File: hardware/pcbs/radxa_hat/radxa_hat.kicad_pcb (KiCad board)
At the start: 2 copper layers, 1 part, among them J1 RADXA_HEADER

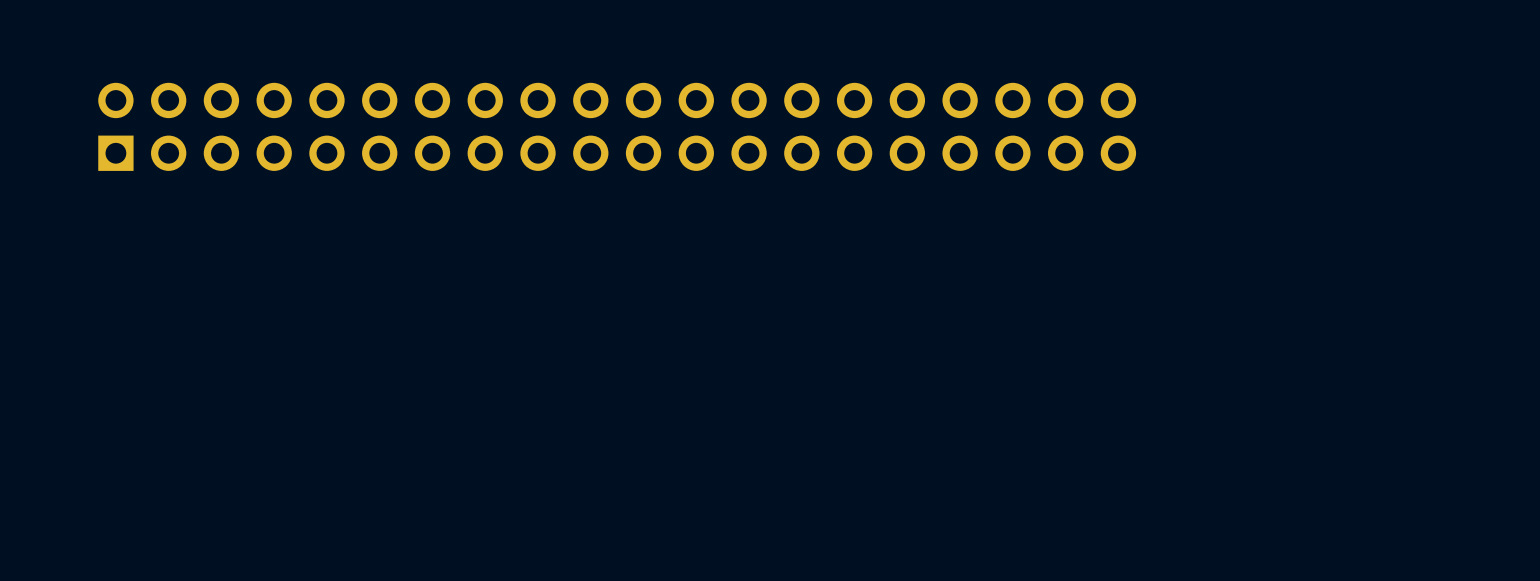
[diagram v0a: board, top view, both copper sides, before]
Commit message: hats_pcbs: add some connectors
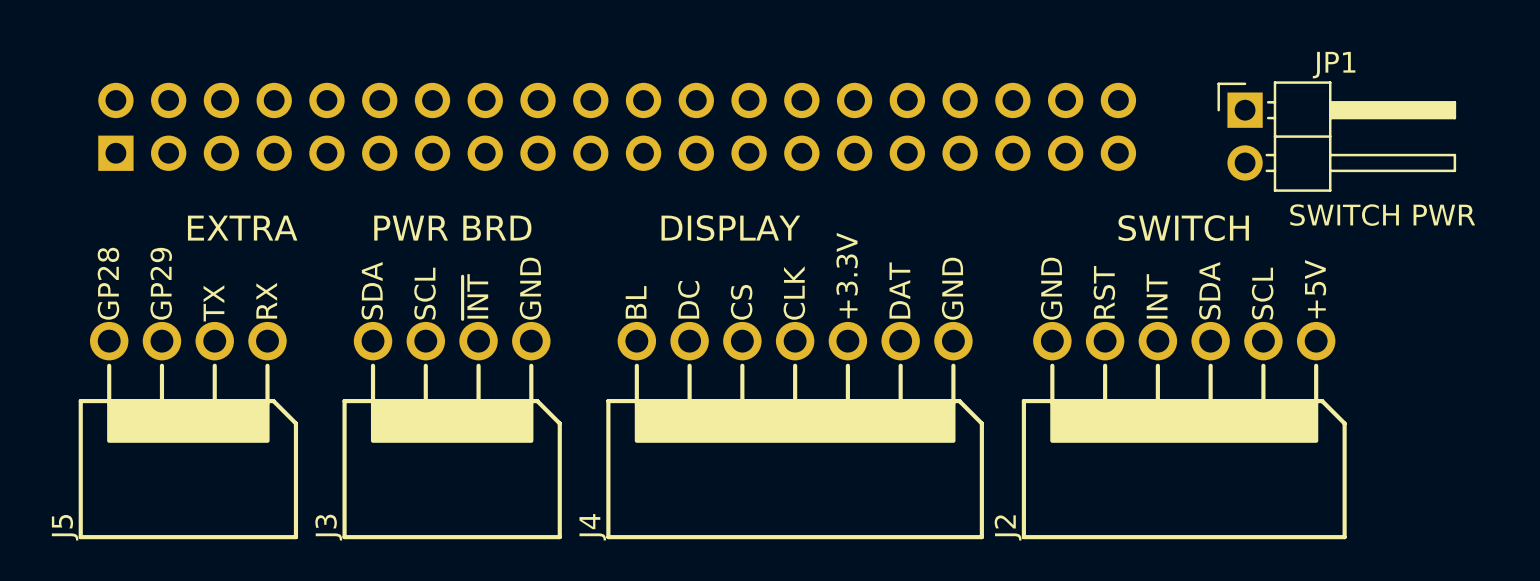
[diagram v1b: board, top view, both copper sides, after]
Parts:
- added J2: Header_01x06, Connector_MTA-100:mta100_01x6_P2.54_640455-6, F.Cu at (132.1, 57.8)
- added J3: Header_01x04, Connector_MTA-100:mta100_01x4_P2.54_640455-4, F.Cu at (99.4, 57.8)
- added J4: Header_01x06, Connector_MTA-100:mta100_01x7_P2.54_640455-7, F.Cu at (112.1, 57.8)
- added J5: Header_01x04, Connector_MTA-100:mta100_01x4_P2.54_640455-4, F.Cu at (86.7, 57.8)
- added JP1: SWITCH PWR, Connector_PinHeader_2.54mm:PinHeader_1x02_P2.54mm_Horizontal, F.Cu at (141.4, 46.7)
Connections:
- J1 pad 1: unconnected-(J1-+3.3V-Pad1) -> +3.3V
- J1 pad 11: unconnected-(J1-GP05-Pad11) -> /EXTRA_RX
- J1 pad 14: unconnected-(J1-GND-Pad14) -> GND
- J1 pad 16: unconnected-(J1-GP22-Pad16) -> /DISP_BL
- J1 pad 17: unconnected-(J1-+3.3V-Pad17) -> +3.3V
- J1 pad 18: unconnected-(J1-GP27-Pad18) -> /PWR_BRD_SCL
- J1 pad 19: unconnected-(J1-GP11-Pad19) -> /DISP_DAT
- J1 pad 2: unconnected-(J1-+5V-Pad2) -> +5V
- J1 pad 20: unconnected-(J1-GND-Pad20) -> GND
- J1 pad 23: unconnected-(J1-GP10-Pad23) -> /DISP_CLK
- J1 pad 25: unconnected-(J1-GND-Pad25) -> GND
- J1 pad 26: unconnected-(J1-GP18-Pad26) -> /PWR_BRD_INT
- J1 pad 28: unconnected-(J1-GP17-Pad28) -> /PWR_BRD_INT
- J1 pad 3: unconnected-(J1-GP28-Pad3) -> /EXTRA_GP28
- J1 pad 30: unconnected-(J1-GND-Pad30) -> GND
- J1 pad 32: unconnected-(J1-GP19-Pad32) -> /DISP_DC
- J1 pad 33: unconnected-(J1-GP13-Pad33) -> /DISP_CS
- J1 pad 34: unconnected-(J1-GND-Pad34) -> GND
- J1 pad 35: unconnected-(J1-GP15-Pad35) -> /NSW_SCL
- J1 pad 36: unconnected-(J1-GP26-Pad36) -> /PWR_BRD_SDA
- J1 pad 37: unconnected-(J1-GP14-Pad37) -> /NSW_SDA
- J1 pad 38: unconnected-(J1-GP02-Pad38) -> /NSW_INT
- J1 pad 39: unconnected-(J1-GND-Pad39) -> GND
- J1 pad 4: unconnected-(J1-+5V-Pad4) -> +5V
- J1 pad 40: unconnected-(J1-GP25-Pad40) -> /NSW_RST
- J1 pad 5: unconnected-(J1-GP29-Pad5) -> /EXTRA_GP29
- J1 pad 6: unconnected-(J1-GND-Pad6) -> GND
- J1 pad 7: unconnected-(J1-GP04-Pad7) -> /EXTRA_TX
- J1 pad 8: unconnected-(J1-GP20-Pad8) -> /DISP_RST
- J1 pad 9: unconnected-(J1-GND-Pad9) -> GND

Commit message: hat_pcbs are almost done
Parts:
- added H1: MountingHole_Pad, MountingHole:MountingHole_3.2mm_M3_DIN965_Pad, F.Cu at (135.0, 88.9)
- added H2: MountingHole_Pad, MountingHole:MountingHole_3.2mm_M3_DIN965_Pad, F.Cu at (77.0, 88.9)
- J4: value Header_01x06 -> Header_01x08; footprint Connector_MTA-100:mta100_01x7_P2.54_640455-7 -> Connector_MTA-100:mta100_01x8_P2.54_640455-8
- JP1: footprint Connector_PinHeader_2.54mm:PinHeader_1x02_P2.54mm_Horizontal -> Connector_PinHeader_2.54mm:PinHeader_1x02_P2.54mm_Vertical
- moved JP1 53.0 mm to (119.4, 94.9)
- moved J3 45.2 mm to (88.3, 101.6)
- moved J4 45.2 mm to (101.0, 101.6)
- moved J5 45.2 mm to (75.6, 101.6)
- moved J2 44.6 mm to (123.8, 101.6)
- moved J1 41.7 mm to (81.9, 90.2)
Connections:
- J2 pad 1: Net-(J2-Pin_1) -> GND
- J2 pad 2: /NSW_SDA -> /NSW_RST
- J2 pad 3: /NSW_SCL -> /NSW_INT
- J2 pad 4: /NSW_INT -> /NSW_SCL
- J2 pad 5: /NSW_RST -> /NSW_SDA
- J2 pad 6: GND -> Net-(J2-Pin_6)
- J3 pad 1: GND -> /PWR_BRD_SDA
- J3 pad 2: /PWR_BRD_INT -> /PWR_BRD_SCL
- J3 pad 3: /PWR_BRD_SCL -> /PWR_BRD_INT
- J3 pad 4: /PWR_BRD_SDA -> GND
- J4 pad 3: /DISP_DAT -> /DISP_CS
- J4 pad 4: /DISP_CLK -> /DISP_DC
- J4 pad 5: /DISP_CS -> /DISP_CLK
- J4 pad 6: /DISP_DC -> /DISP_DAT
- JP1 pad 1: Net-(J2-Pin_1) -> Net-(J2-Pin_6)
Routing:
- net +3.3V: track 0.00 -> 68.8 mm
- net +5V: track 0.00 -> 63.5 mm
- net /PWR_BRD_SDA: track 0.00 -> 40.7 mm
- net /PWR_BRD_INT: track 0.00 -> 35.4 mm, vias 0 -> 1
- net /DISP_DC: track 0.00 -> 20.3 mm
- net /DISP_RST: track 0.00 -> 20.2 mm
- net /EXTRA_RX: track 0.00 -> 19.0 mm
- net /DISP_CS: track 0.00 -> 18.8 mm
- net /EXTRA_GP29: track 0.00 -> 18.6 mm
- net /EXTRA_GP28: track 0.00 -> 18.6 mm
- net /EXTRA_TX: track 0.00 -> 17.7 mm
- net /PWR_BRD_SCL: track 0.00 -> 17.7 mm
- net /NSW_SCL: track 0.00 -> 16.6 mm
- net /DISP_BL: track 0.00 -> 15.5 mm
- net /NSW_RST: track 0.00 -> 15.5 mm
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- added copper zone on B.Cu, net GND
- added copper zone on F.Cu, net GND
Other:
- board outline added: 65 x 26.5 mm

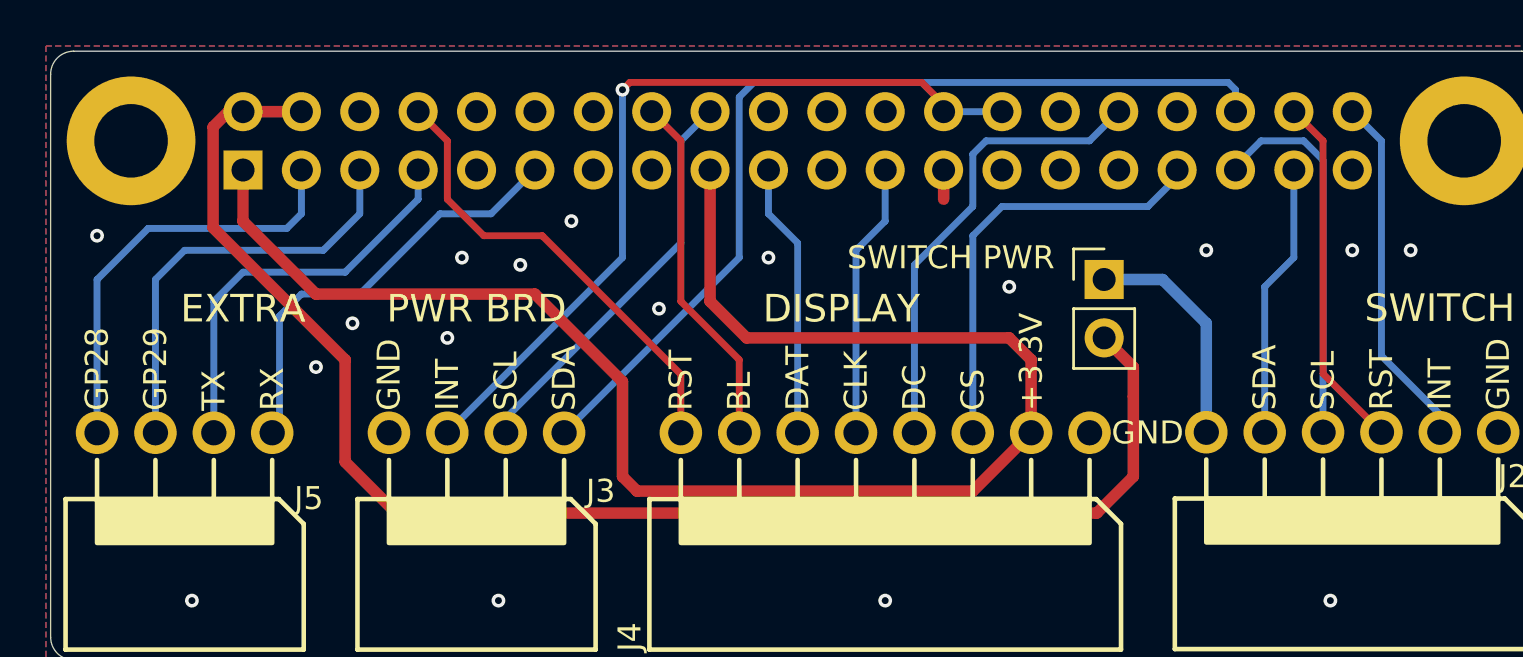
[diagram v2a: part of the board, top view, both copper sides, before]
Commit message: hat_pcbs: add some resistors
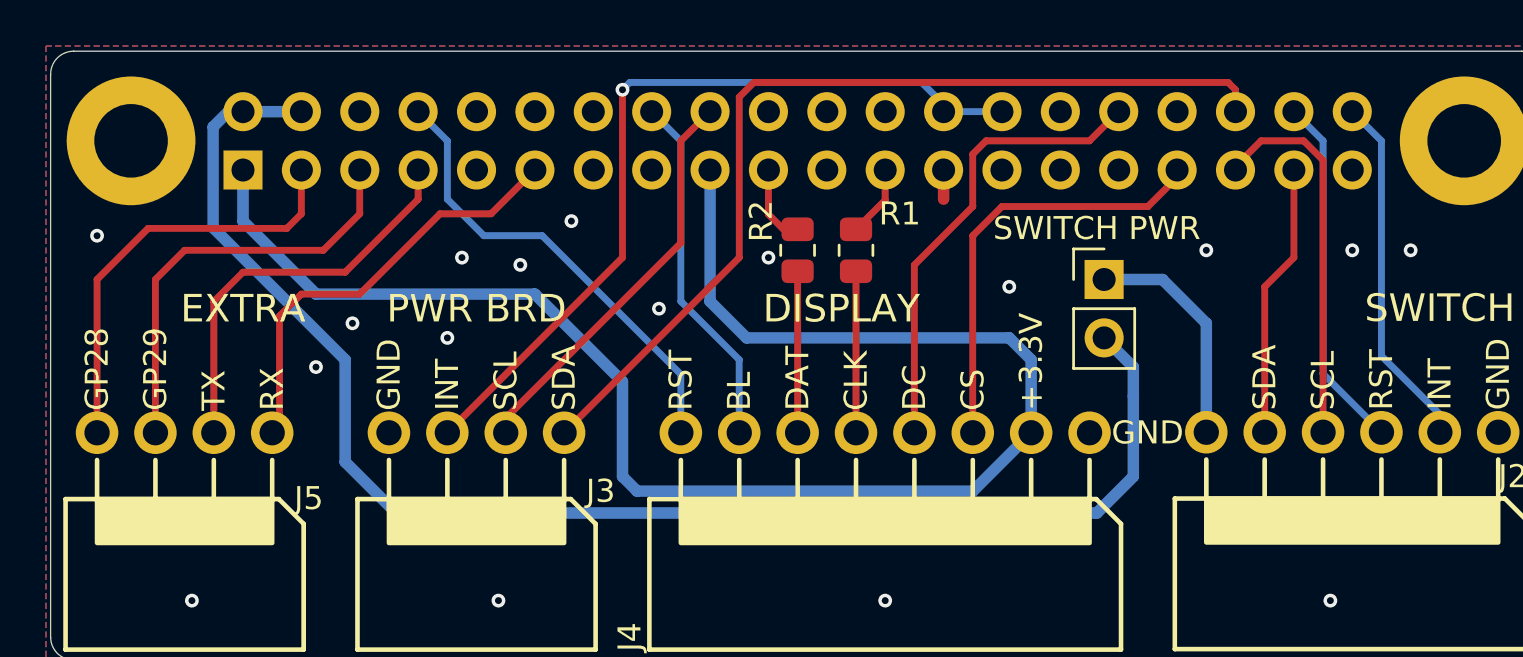
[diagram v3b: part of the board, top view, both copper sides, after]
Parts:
- added R1: 1Ω, Resistor_SMD:R_0805_2012Metric, F.Cu at (108.6, 93.7)
- added R2: 1Ω, Resistor_SMD:R_0805_2012Metric, F.Cu at (106.0, 93.7)
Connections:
- J4 pad 5: /DISP_CLK -> Net-(J4-Pin_5)
- J4 pad 6: /DISP_DAT -> Net-(J4-Pin_6)
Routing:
- net /DISP_CLK: track 12.0 -> 3.11 mm
- net /DISP_DAT: track 12.0 -> 3.47 mm
- net Net-(J4-Pin_6): track 0.00 -> 7.02 mm
- net Net-(J4-Pin_5): track 0.00 -> 7.02 mm

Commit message: hat_pcbs: final changes
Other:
- board text added: "FOSDEM radxa hat rev. A"
- board text added: "JLCJLCJLCJLC"
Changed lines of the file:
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@@
 	)
 	(paper "A4")
+	(title_block
+		(comment 4 "AISLER Project ID: AAMJXCDQ")
+	)
 	(layers
 		(0 "F.Cu" signal)
@@
 		(layer "Edge.Cuts")
 	)
+	(gr_text "JLCJLCJLCJLC"
+		(at 95.25 105.7275 180)
+		(layer "B.SilkS")
+		(effects
+			(font
+				(size 1 1)
+				(thickness 0.1)
+			)
+			(justify left bottom mirror)
+		)
+	)
+	(gr_text "FOSDEM radxa hat rev. A"
+		(at 90.4875 107.315 180)
+		(layer "B.SilkS")
+		(effects
+			(font
+				(size 1 1)
+				(thickness 0.1)
+			)
+			(justify left bottom mirror)
+		)
+	)
 	(segment

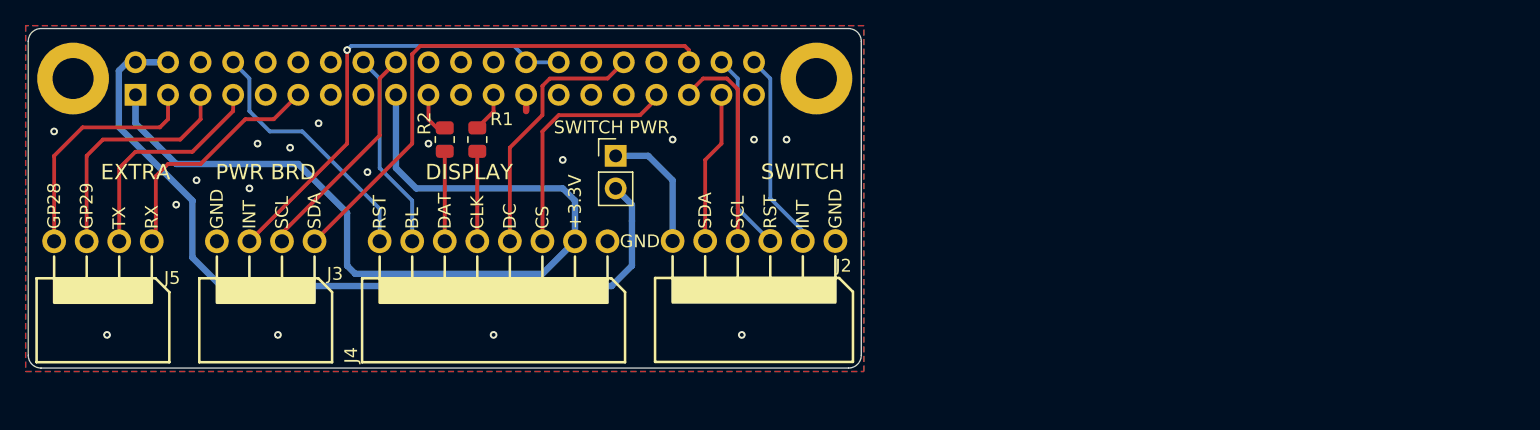
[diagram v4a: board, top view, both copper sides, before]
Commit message: boards: update fabrication output settings
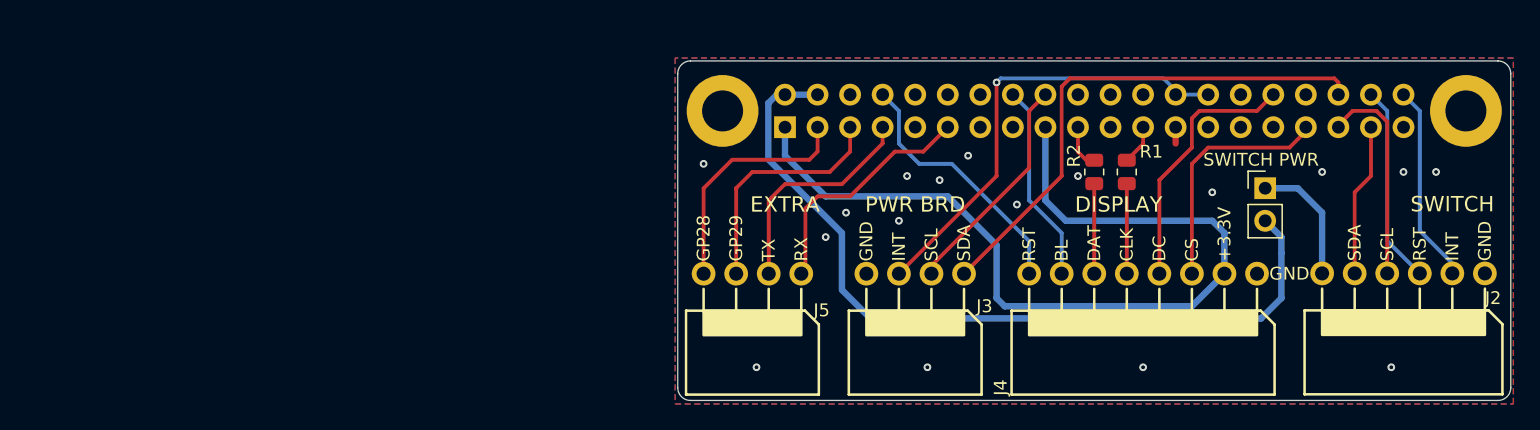
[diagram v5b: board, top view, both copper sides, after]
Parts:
- moved H1 50.7 mm to (185.7, 91.4)
- moved J4 50.7 mm to (151.6, 104.1)
- moved J5 50.7 mm to (126.2, 104.1)
- moved JP1 50.7 mm to (170.1, 97.5)
- moved H2 50.7 mm to (127.7, 91.4)
- moved J1 50.7 mm to (132.6, 92.7)
- moved J2 50.7 mm to (174.5, 104.1)
- moved J3 50.7 mm to (138.9, 104.1)
- moved R1 50.7 mm to (159.3, 96.2)
- moved R2 50.7 mm to (156.7, 96.2)

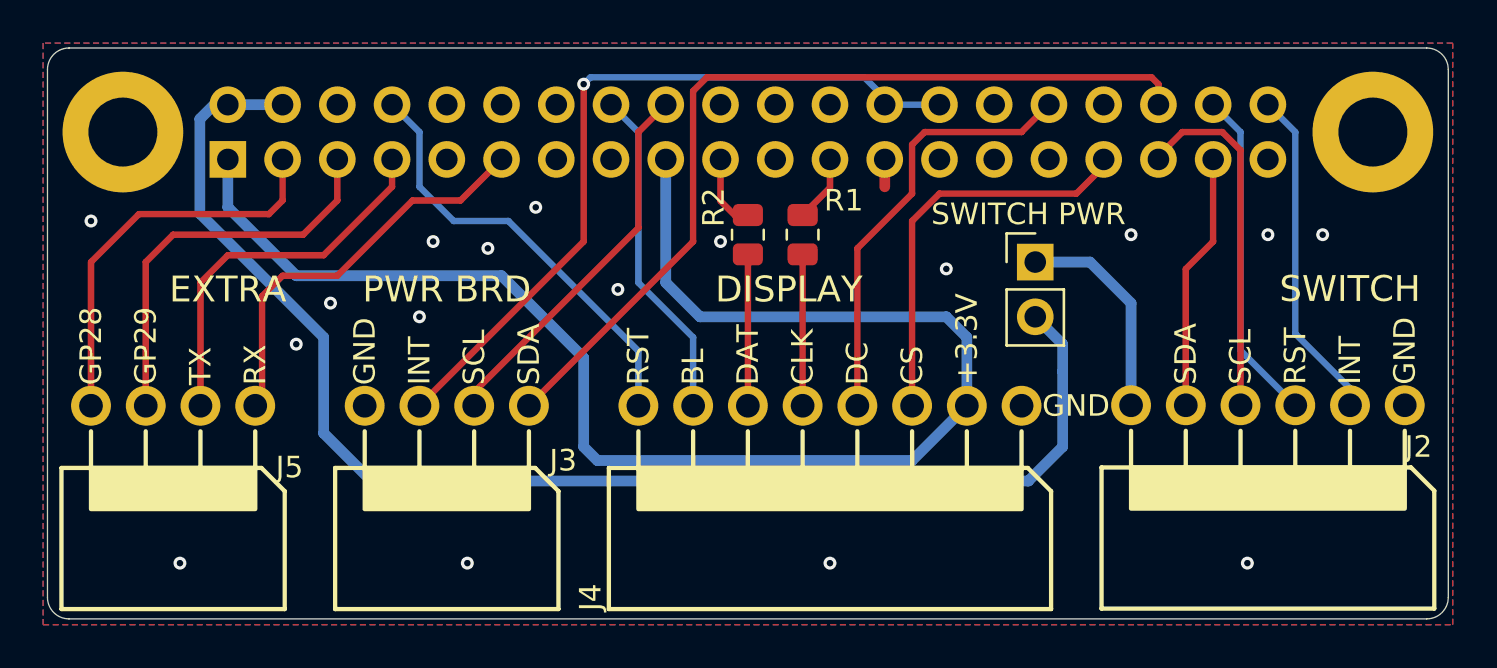
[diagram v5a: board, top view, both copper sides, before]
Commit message: boards: fix many silly bugs discovered during testing
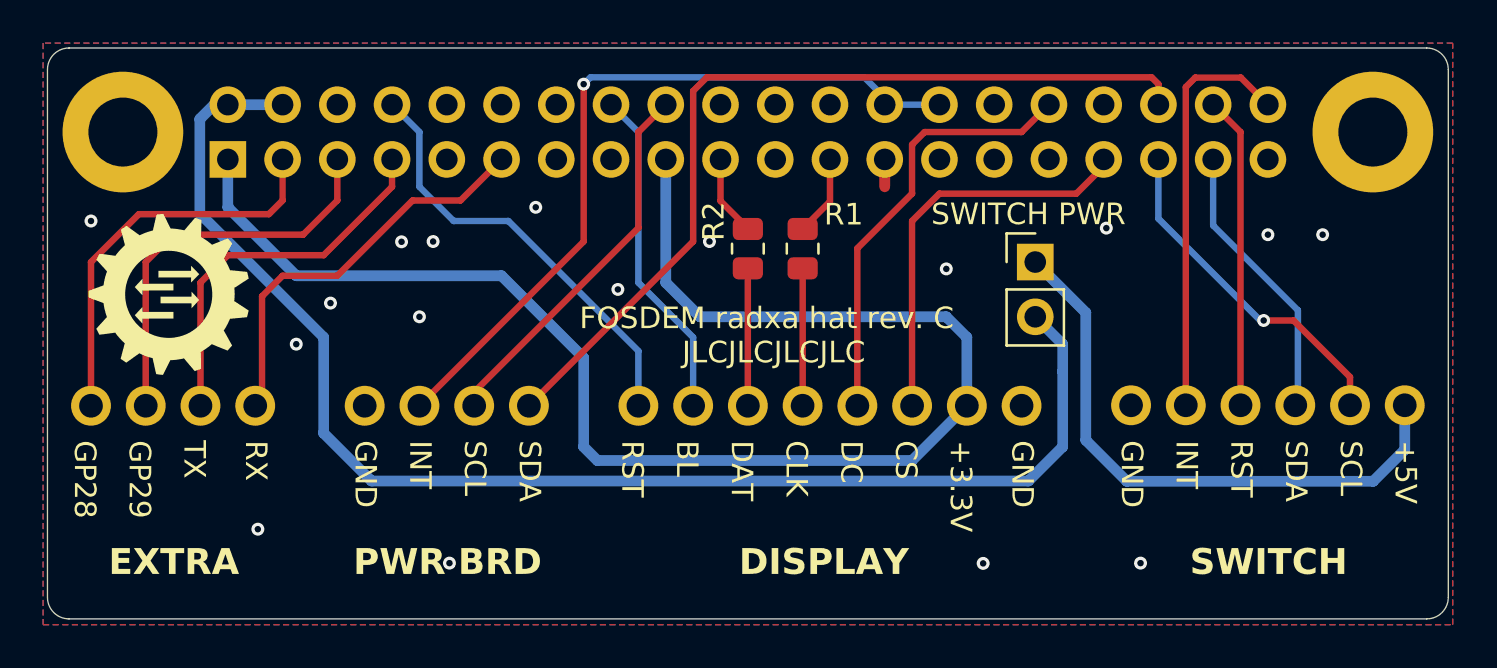
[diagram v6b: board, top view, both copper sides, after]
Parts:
- J2, J3, J4, J5: moved to B.Cu
- moved J4 17.8 mm to (169.4, 104.1), turned to 180 degrees
- moved J2 12.7 mm to (187.2, 104.1), turned to 180 degrees
- moved J3 7.62 mm to (146.6, 104.1), turned to 180 degrees
- moved J5 7.62 mm to (133.9, 104.1), turned to 180 degrees
- moved R1 0.65 mm to (159.3, 96.8)
- moved R2 0.65 mm to (156.7, 96.8)
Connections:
- J2 pad 4: /NSW_SCL -> /NSW_SDA
- J2 pad 5: /NSW_SDA -> /NSW_SCL
- J3 pad 1: /PWR_BRD_SDA -> GND
- J3 pad 2: /PWR_BRD_SCL -> /PWR_BRD_INT
- J3 pad 3: /PWR_BRD_INT -> /PWR_BRD_SCL
- J3 pad 4: GND -> /PWR_BRD_SDA
- J4 pad 1: GND -> /DISP_RST
- J4 pad 2: +3.3V -> /DISP_BL
- J4 pad 3: /DISP_CS -> Net-(J4-Pin_3)
- J4 pad 4: /DISP_DC -> Net-(J4-Pin_4)
- J4 pad 5: Net-(J4-Pin_5) -> /DISP_DC
- J4 pad 6: Net-(J4-Pin_6) -> /DISP_CS
- J4 pad 7: /DISP_BL -> +3.3V
- J4 pad 8: /DISP_RST -> GND
- J5 pad 1: /EXTRA_RX -> /EXTRA_GP28
- J5 pad 2: /EXTRA_TX -> /EXTRA_GP29
- J5 pad 3: /EXTRA_GP29 -> /EXTRA_TX
- J5 pad 4: /EXTRA_GP28 -> /EXTRA_RX
- R1 pad 2: Net-(J4-Pin_5) -> Net-(J4-Pin_4)
- R2 pad 2: Net-(J4-Pin_6) -> Net-(J4-Pin_3)
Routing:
- net Net-(J2-Pin_6): track 9.97 -> 27.5 mm
- net Net-(J4-Pin_6): track 7.02 -> 0.00 mm
- net Net-(J4-Pin_5): track 7.02 -> 0.00 mm
- net Net-(J4-Pin_4): track 0.00 -> 6.38 mm
- net Net-(J4-Pin_3): track 0.00 -> 6.38 mm
- net /NSW_RST: track 15.5 -> 19.3 mm
- net /NSW_SDA: track 11.9 -> 13.1 mm
- net /NSW_INT: track 15.5 -> 14.5 mm
- net /DISP_CLK: track 3.11 -> 3.75 mm
- net /NSW_SCL: track 16.6 -> 16.0 mm, vias 0 -> 1
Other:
- board text added: "+3.3V"
- board text added: "+5V"
- board text added: "BL"
- board text added: "CLK"
- board text added: "CS"
- board text added: "DAT"
- board text added: "DC"
- board text added: "DISPLAY"
- board text added: "EXTRA"
- board text added: "FOSDEM radxa hat rev. C"
- board text added: "GND"
- board text added: "GP28"
- board text added: "GP29"
- board text added: "INT"
- board text added: "PWR BRD"
- board text added: "RST"
- board text added: "RX"
- board text added: "SCL"
- board text added: "SDA"
- board text added: "SWITCH"
- board text added: "TX"
- board text removed: "FOSDEM radxa hat rev. A"
